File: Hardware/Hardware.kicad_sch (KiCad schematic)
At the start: 0 parts

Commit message: feat: add project
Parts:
- added BT1: Battery_Cell, symbol Device:Battery_Cell
- added D1, D2: LED, symbol Device:LED
- added D3: LED, Connector_PinHeader_1.27mm:PinHeader_1x02_P1.27mm_Vertical, symbol Device:LED
- added J1: USB_C_Receptacle_USB2.0_16P, symbol Connector:USB_C_Receptacle_USB2.0_16P
- added Q1: AO3400A, Package_TO_SOT_SMD:SOT-23, symbol Transistor_FET:AO3400A
- added R1, R2, R3, R4, R5: R, symbol Device:R
- added SW1: SW_Nidec_CAS-120A1, Button_Switch_SMD:SW_SPDT_PCM12, symbol Switch:SW_Nidec_CAS-120A1
- added U1: CH32V003FxPx, Package_SO:TSSOP-20_4.4x6.5mm_P0.65mm, symbol MCU_WCH_RiscV:CH32V003FxPx
- added U2: AMS1117-3.3, Package_TO_SOT_SMD:SOT-223-3_TabPin2, symbol Regulator_Linear:AMS1117-3.3
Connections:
- new net: D1.1 (K), D2.1 (K), D3.1 (K), Q1.2 (S)
- new net: D2.2 (A), R2.2
- new net: D1.2 (A), R1.2
- new net: Q1.1 (G), R4.1, R5.1
- new net: D3.2 (A), R3.2
- new net +3.3V: R1.1, R2.1, R3.1, U1.9 (VDD), U2.2 (VO)
- new net GND: J1.A1 (GND), J1.A12 (GND), J1.B1 (GND), J1.B12 (GND), J1.SH (SHIELD), Q1.3 (D), R5.2, U1.7 (VSS), U2.1 (GND)
- new net VBUS: J1.A4 (VBUS), J1.A9 (VBUS), J1.B4 (VBUS), J1.B9 (VBUS), U2.3 (VI)
- new net control: R4.2
- no-connect marks 0 -> 8

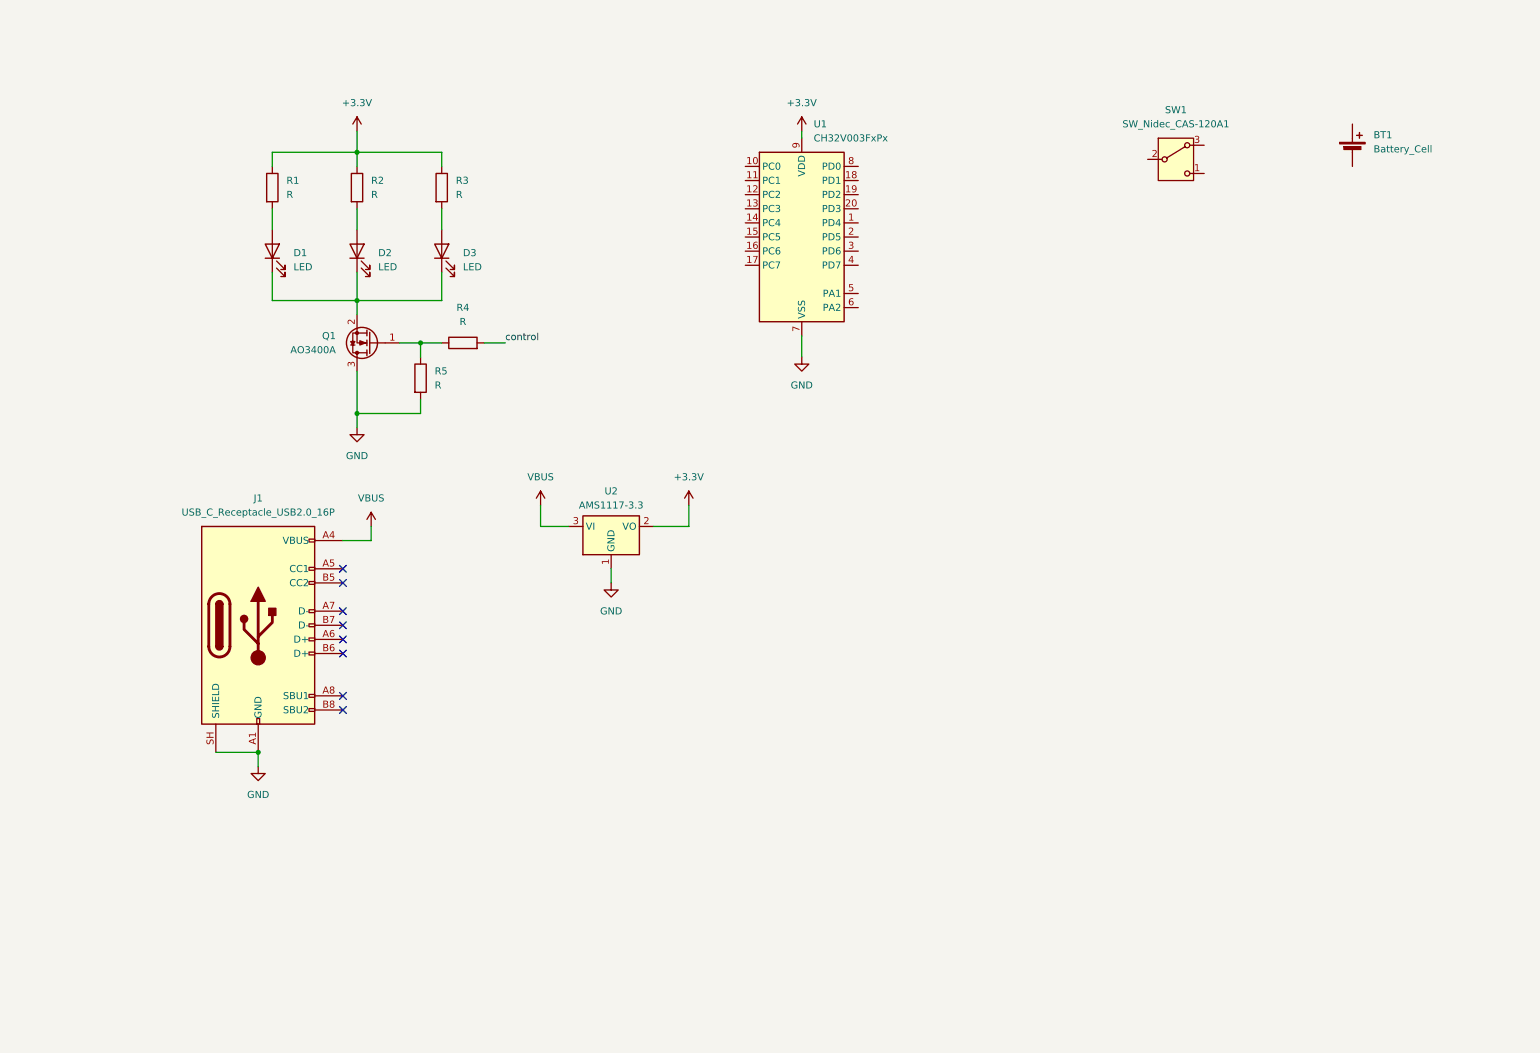
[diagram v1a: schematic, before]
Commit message: feat: add components on schematic file
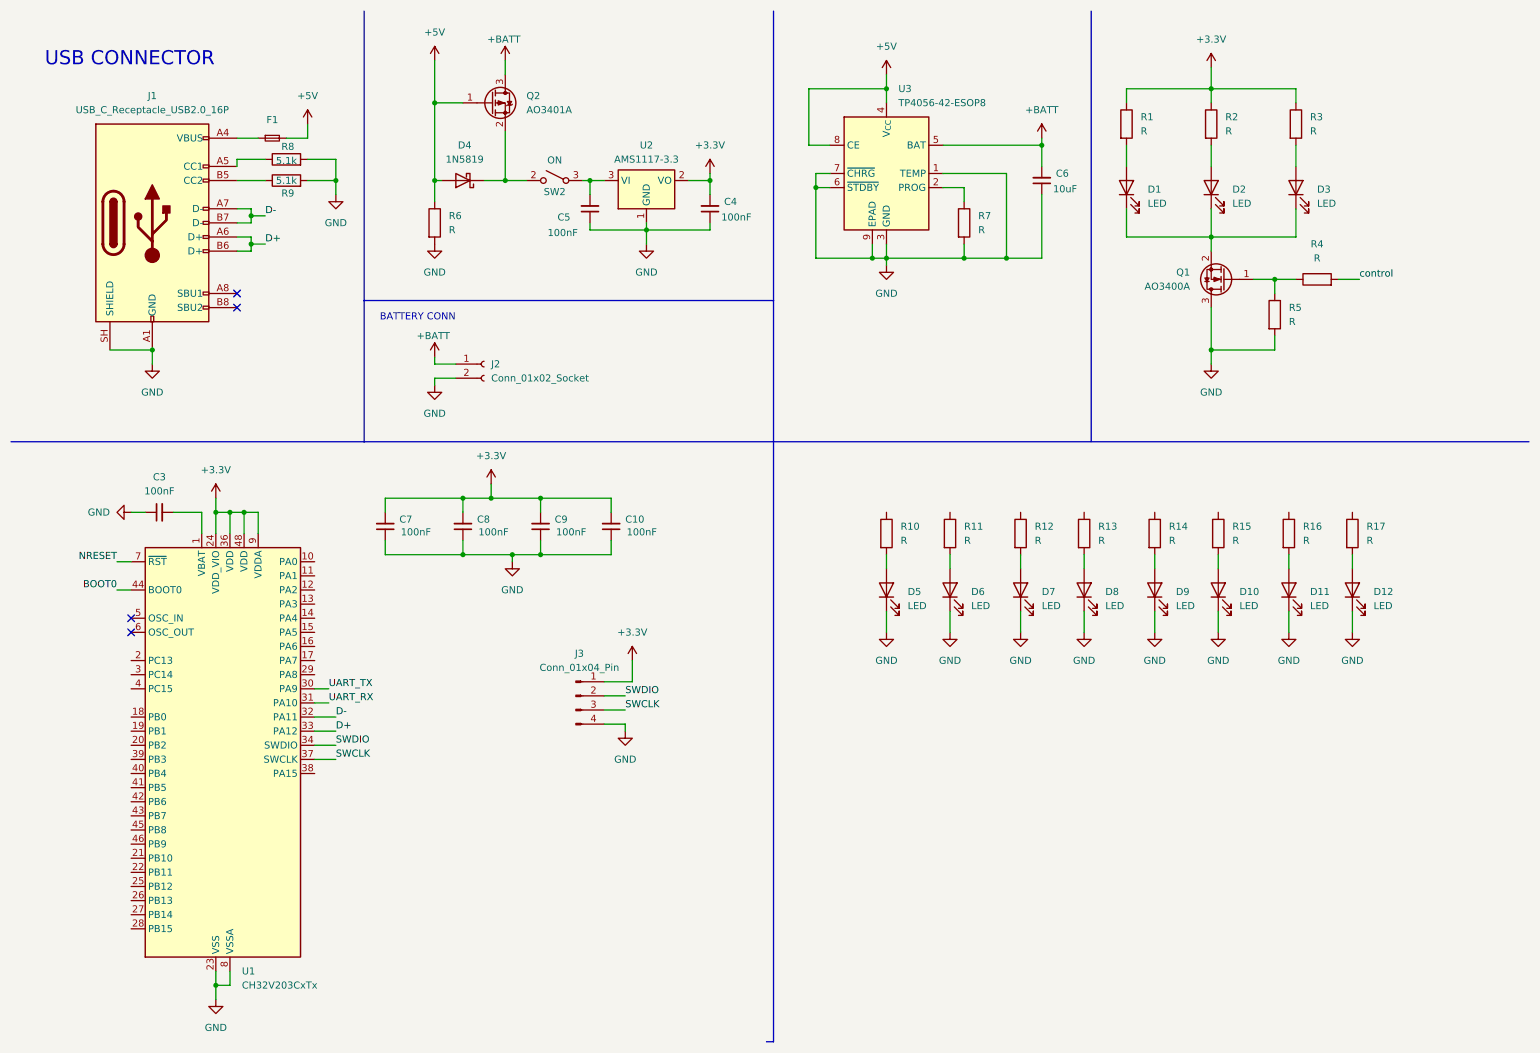
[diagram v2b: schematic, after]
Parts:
- removed BT1: Battery_Cell, symbol Device:Battery_Cell
- removed SW1: SW_Nidec_CAS-120A1, Button_Switch_SMD:SW_SPDT_PCM12, symbol Switch:SW_Nidec_CAS-120A1
- removed U1: CH32V003FxPx, Package_SO:TSSOP-20_4.4x6.5mm_P0.65mm, symbol MCU_WCH_RiscV:CH32V003FxPx
- added C10, C3, C4, C5, C7, C8, C9: 100nF, Capacitor_SMD:C_0805_2012Metric, symbol Device:C_Small
- added C6: 10uF, Capacitor_SMD:C_0805_2012Metric, symbol Device:C_Small
- added D10, D11, D12, D5, D6, D7, D8, D9: LED, LED_SMD:LED_Cree-XHP50_3V_HighDensity, symbol Device:LED
- added D4: 1N5819, Diode_THT:D_DO-41_SOD81_P10.16mm_Horizontal, symbol Diode:1N5819
- added F1: Fuse_Small, Package_SO:SOIC-8-1EP_3.9x4.9mm_P1.27mm_EP2.41x3.3mm_ThermalVias, symbol Device:Fuse_Small
- added J2: Conn_01x02_Socket, Package_DFN_QFN:QFN-40-1EP_6x6mm_P0.5mm_EP4.6x4.6mm, symbol Connector:Conn_01x02_Socket
- added J3: Conn_01x04_Pin, symbol Connector:Conn_01x04_Pin
- added Q2: AO3401A, Package_TO_SOT_SMD:SOT-23, symbol Transistor_FET:AO3401A
- added R10, R11, R12, R13, R14, R15, R16, R17, R7: R, symbol Device:R
- added R6: R, Package_TO_SOT_SMD:SOT-223-3_TabPin2, symbol Device:R
- added R8, R9: 5.1k, Resistor_SMD:R_0805_2012Metric, symbol Device:R
- added SW2: ON, Footprints:MSK12C02, symbol Switch:SW_SPST
- added U1: CH32V203CxTx, Package_QFP:LQFP-48_7x7mm_P0.5mm, symbol MCU_WCH_RiscV:CH32V203CxTx
- added U3: TP4056-42-ESOP8, Package_SO:SOIC-8-1EP_3.9x4.9mm_P1.27mm_EP2.41x3.3mm_ThermalVias, symbol Battery_Management:TP4056-42-ESOP8
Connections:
- net +3.3V: now also C10.2, C4.2, C7.2, C8.2, C9.2, J3.1 (Pin_1), U1.24 (VDD_VIO), U1.36 (VDD), U1.48 (VDD), U1.9 (VDDA)
- net GND: now also C10.1, C3.1, C4.1, C5.1, C6.1, C7.1, C8.1, C9.1, D10.1 (K), D11.1 (K), D12.1 (K), D5.1 (K), D6.1 (K), D7.1 (K), D8.1 (K), D9.1 (K), J2.2 (Pin_2), J3.4 (Pin_4), R6.2, R7.2, R8.2, R9.2, U1.23 (VSS), U1.35 (VSS), U1.47 (VSS), U1.8 (VSSA), U3.1 (TEMP), U3.3 (GND), U3.6 (~{STDBY}), U3.7 (~{CHRG}), U3.9 (EPAD)
- net at J1.A5 (CC1): now also R8.1
- net D+: now reaches J1.A6 (D+)
- net D+: now also J1.B6 (D+), U1.33 (PA12)
- net D-: now reaches J1.A7 (D-)
- net D-: now also J1.B7 (D-), U1.32 (PA11)
- net at J1.B5 (CC2): now also R9.1
- net VBUS: no longer names the net of J1.A4 (VBUS), J1.A9 (VBUS), J1.B4 (VBUS), J1.B9 (VBUS)
- net VBUS: now also F1.1; no longer U2.3 (VI)
- new net: D4.1 (K), Q2.2 (S), SW2.2 (B)
- new net: C5.2, SW2.3 (A), U2.3 (VI)
- new net: D5.2 (A), R10.2
- new net: D12.2 (A), R17.2
- new net: D6.2 (A), R11.2
- new net: D7.2 (A), R12.2
- new net: D10.2 (A), R15.2
- new net: R7.1, U3.2 (PROG)
- new net: D9.2 (A), R14.2
- new net: D8.2 (A), R13.2
- new net: C3.2, U1.1 (VBAT)
- new net: D11.2 (A), R16.2
- new net +5V: D4.2 (A), F1.2, Q2.1 (G), R6.1, U3.4 (V_{CC}), U3.8 (CE)
- new net +BATT: C6.2, J2.1 (Pin_1), Q2.3 (D), U3.5 (BAT)
- new net BOOT0: U1.44 (BOOT0)
- new net NRESET: U1.7 (~{RST})
- new net SWCLK: J3.3 (Pin_3), U1.37 (SWCLK)
- new net SWDIO: J3.2 (Pin_2), U1.34 (SWDIO)
- new net UART_RX: U1.31 (PA10)
- new net UART_TX: U1.30 (PA9)
- no-connect marks 8 -> 4
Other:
- note added: "BATTERY CONN"
- note added: "USB CONNECTOR"
- moved on the sheet: D1, D2, D3, J1, Q1, R1, R2, R3, R4, R5

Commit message: feat: add components on pcb
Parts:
- added C11, C12: 100nF, Capacitor_SMD:C_0805_2012Metric, symbol Device:C_Small
- added D13, D14: LED, LED_SMD:LED_0603_1608Metric, symbol Device:LED
- added R18, R19: 660, Resistor_SMD:R_0805_2012Metric, symbol Device:R
- added U4: AMS1117-3.3, Package_TO_SOT_SMD:SOT-223-3_TabPin2, symbol Regulator_Linear:AMS1117-3.3
- D1, D2: footprint (none) -> Connector_PinHeader_1.27mm:PinHeader_1x02_P1.27mm_Vertical
- D10, D11, D12, D5, D6, D7, D8, D9: footprint LED_SMD:LED_Cree-XHP50_3V_HighDensity -> LED_SMD:LED_0603_1608Metric
- D4: footprint Diode_THT:D_DO-41_SOD81_P10.16mm_Horizontal -> Diode_SMD:D_SOD-323
- F1: footprint Package_SO:SOIC-8-1EP_3.9x4.9mm_P1.27mm_EP2.41x3.3mm_ThermalVias -> Fuse:Fuse_0603_1608Metric
- J1: footprint (none) -> Connector_USB:USB_C_Receptacle_Palconn_UTC16-G
- J2: footprint Package_DFN_QFN:QFN-40-1EP_6x6mm_P0.5mm_EP4.6x4.6mm -> Connector_JST:JST_PH_S2B-PH-SM4-TB_1x02-1MP_P2.00mm_Horizontal
- J3: footprint (none) -> Connector_PinHeader_2.54mm:PinHeader_1x04_P2.54mm_Vertical
- R1, R2, R3: value R -> 33; footprint (none) -> Resistor_SMD:R_0805_2012Metric
- R10, R11, R12, R13, R14, R15, R16, R17: value R -> 660; footprint (none) -> Resistor_SMD:R_0805_2012Metric
- R4: value R -> 10; footprint (none) -> Resistor_SMD:R_0805_2012Metric
- R5: value R -> 10k; footprint (none) -> Resistor_SMD:R_0805_2012Metric
- R6: value R -> 10k; footprint Package_TO_SOT_SMD:SOT-223-3_TabPin2 -> Resistor_SMD:R_0805_2012Metric
- R7: value R -> 1.2K; footprint (none) -> Resistor_SMD:R_0805_2012Metric
- SW2: footprint Footprints:MSK12C02 -> Button_Switch_SMD:SW_SPDT_Shouhan_MSK12C02
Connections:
- net +3.3V: no longer R1.1, R2.1, R3.1
- net +BATT: now also J2.2 (Pin_2); no longer J2.1 (Pin_1)
- net GND: now also J2.1 (Pin_1), C11.1, C12.1, D13.1 (K), D14.1 (K), U4.1 (GND); no longer J2.2 (Pin_2)
- net control: now also U1.21 (PB10)
- net OUT: now reaches C5.2, SW2.3 (A), U2.3 (VI)
- net OUT: now also C11.2, U4.3 (VI)
- net LED_1: now reaches R10.1
- net LED_1: now also U1.18 (PB0)
- net LED_2: now reaches R11.1
- net LED_2: now also U1.19 (PB1)
- net LED_3: now reaches R12.1
- net LED_3: now also U1.20 (PB2)
- net LED_6: now reaches R15.1
- net LED_6: now also U1.41 (PB5)
- net LED_8: now reaches R17.1
- net LED_8: now also U1.43 (PB7)
- net LED_5: now reaches R14.1
- net LED_5: now also U1.40 (PB4)
- net LED_4: now reaches U1.39 (PB3)
- net LED_4: now also R13.1
- net LED_7: now reaches U1.42 (PB6)
- net LED_7: now also R16.1
- net LED_9: now reaches U1.45 (PB8)
- net LED_9: now also R18.1
- net LED_10: now reaches U1.46 (PB9)
- net LED_10: now also R19.1
- net UART_RX: no longer names the net of U1.31 (PA10)
- net UART_TX: no longer names the net of U1.30 (PA9)
- new net: D13.2 (A), R18.2
- new net: D14.2 (A), R19.2
- new net +3V3: C12.2, R1.1, R2.1, R3.1, U4.2 (VO)
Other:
- moved on the sheet: C4, C5, D10, D11, D12, D5, D6, D7, D8, D9, R10, R11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

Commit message: feat: set component position
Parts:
- added C13: 10uF, Capacitor_SMD:C_0805_2012Metric, symbol Device:C_Small
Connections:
- net +5V: now also C13.2
- net GND: now also C13.1
- net OUT: now also SW2.2 (B); no longer SW2.3 (A)
- net at D4.1 (K), Q2.2 (S): now also SW2.3 (A); no longer SW2.2 (B)
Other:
- moved on the sheet: C6, SW2

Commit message: feat: add routes
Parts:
- added R20, R21: 10k, Resistor_SMD:R_0805_2012Metric, symbol Device:R
- added SW1, SW3: SW_Push, Button_Switch_SMD:SW_SPST_PTS810, symbol Switch:SW_Push
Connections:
- net +3.3V: now also R20.2, SW3.2
- net BOOT0: now also R21.1, SW3.1
- net GND: now also R21.2, SW1.1
- net LED_1: now also U1.4 (PC15); no longer U1.18 (PB0)
- net LED_10: now also U1.39 (PB3); no longer U1.46 (PB9)
- net LED_2: now also U1.3 (PC14); no longer U1.19 (PB1)
- net LED_3: now also U1.2 (PC13); no longer U1.20 (PB2)
- net LED_4: now also U1.46 (PB9); no longer U1.39 (PB3)
- net LED_5: now also U1.45 (PB8); no longer U1.40 (PB4)
- net LED_6: now also U1.43 (PB7); no longer U1.41 (PB5)
- net LED_8: now also U1.41 (PB5); no longer U1.43 (PB7)
- net LED_9: now also U1.40 (PB4); no longer U1.45 (PB8)
- net NRESET: now also R20.1, SW1.2
- net control: now also U1.10 (PA0); no longer U1.21 (PB10)

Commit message: feat: finish routes
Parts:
- D1, D2, D3: footprint Connector_PinHeader_1.27mm:PinHeader_1x02_P1.27mm_Vertical -> Connector_PinHeader_2.54mm:PinHeader_1x02_P2.54mm_Vertical
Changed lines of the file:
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@@
 			)
 		)
-		(property "Footprint" "Connector_PinHeader_1.27mm:PinHeader_1x02_P1.27mm_Vertical"
+		(property "Footprint" "Connector_PinHeader_2.54mm:PinHeader_1x02_P2.54mm_Vertical"
 			(at 227.33 44.45 0)
 			(hide yes)
@@
 			)
 		)
-		(property "Footprint" "Connector_PinHeader_1.27mm:PinHeader_1x02_P1.27mm_Vertical"
+		(property "Footprint" "Connector_PinHeader_2.54mm:PinHeader_1x02_P2.54mm_Vertical"
 			(at 212.09 44.45 0)
 			(hide yes)
@@
 			)
 		)
-		(property "Footprint" "Connector_PinHeader_1.27mm:PinHeader_1x02_P1.27mm_Vertical"
+		(property "Footprint" "Connector_PinHeader_2.54mm:PinHeader_1x02_P2.54mm_Vertical"
 			(at 242.57 44.45 0)
 			(hide yes)
